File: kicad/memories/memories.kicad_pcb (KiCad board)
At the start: 2 copper layers, 3 parts, among them J1 Conn_01x08, J2 Conn_01x08, U1 NAND512

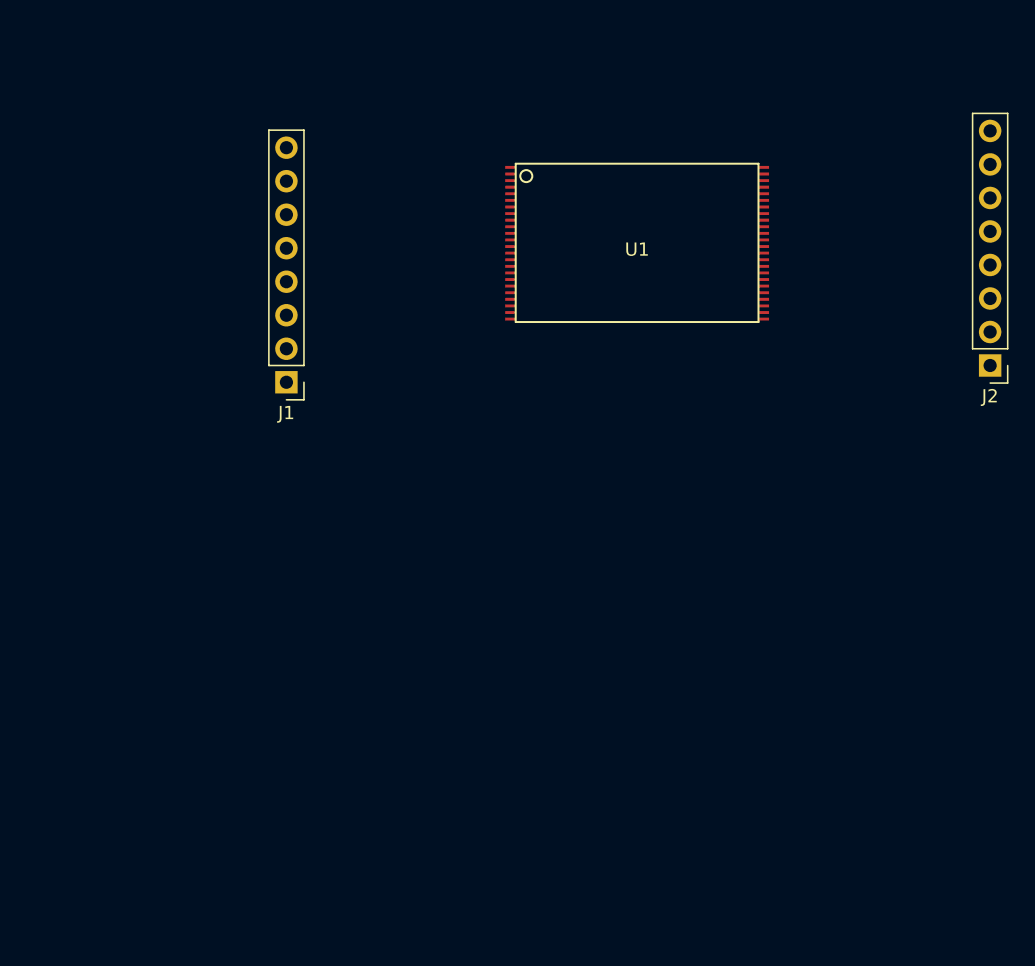
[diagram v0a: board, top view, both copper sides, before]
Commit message: kicad: add mojo shield.
It contains SDRAM, Flash, VGA and PS2.
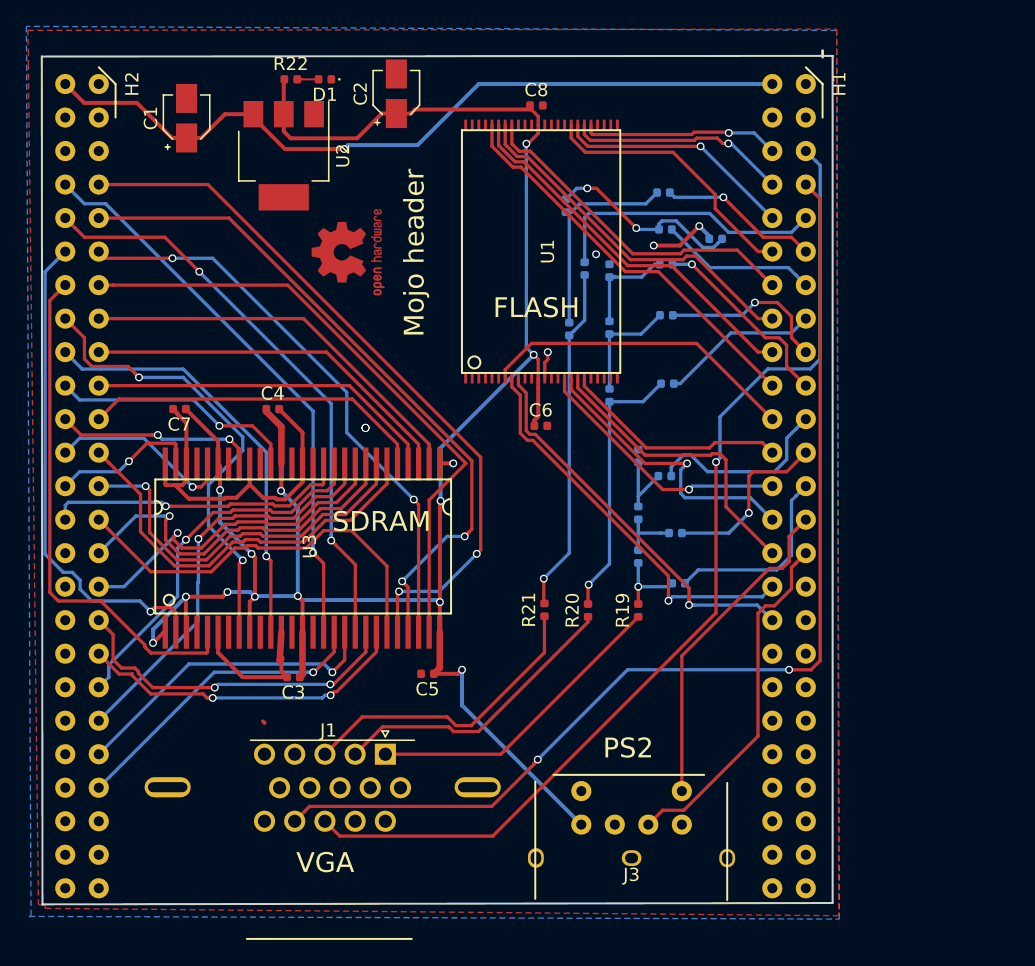
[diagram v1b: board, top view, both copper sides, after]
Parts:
- removed J2: Conn_01x08, Pin_Headers:Pin_Header_Straight_1x08_Pitch2.54mm
- added C1: CP1, Capacitor_SMD:CP_Elec_3x5.3, F.Cu at (114.4, 95.6)
- added C2: CP1, Capacitor_SMD:CP_Elec_3x5.3, F.Cu at (130.3, 93.7)
- added C3: C, Capacitor_SMD:C_0402_1005Metric, F.Cu at (122.5, 137.9)
- added C4: C, Capacitor_SMD:C_0402_1005Metric, F.Cu at (120.9, 117.6)
- added C5: C, Capacitor_SMD:C_0402_1005Metric, F.Cu at (132.6, 137.7)
- added C6: C, Capacitor_SMD:C_0402_1005Metric, F.Cu at (141.2, 118.9)
- added C7: C, Capacitor_SMD:C_0402_1005Metric, F.Cu at (113.8, 117.6)
- added C8: C, Capacitor_SMD:C_0402_1005Metric, F.Cu at (140.9, 94.6)
- added D1: LED, LED_SMD:LED_0402_1005Metric, F.Cu at (124.8, 92.6)
- added H1: Header, memories:mojo_header, F.Cu at (146.1, 100.6)
- added H2: mojo_header_lower, memories:mojo_header, F.Cu at (92.5, 100.6)
- added J3: DIN-6, memories:mini-DIN6, F.Cu at (148.1, 147.8)
- added R1: R, Resistor_SMD:R_0402_1005Metric, B.Cu at (150.6, 122.7)
- added R10: R, Resistor_SMD:R_0402_1005Metric, B.Cu at (151.4, 127.0)
- added R11: R, Resistor_SMD:R_0402_1005Metric, B.Cu at (150.7, 110.5)
- added R12: R, Resistor_SMD:R_0402_1005Metric, B.Cu at (150.5, 101.2)
- added R13: R, Resistor_SMD:R_0402_1005Metric, B.Cu at (148.6, 128.8)
- added R14: R, Resistor_SMD:R_0402_1005Metric, B.Cu at (146.4, 116.6)
- added R15: R, Resistor_SMD:R_0402_1005Metric, B.Cu at (143.4, 111.5)
- added R16: R, Resistor_SMD:R_0402_1005Metric, B.Cu at (151.6, 130.8)
- added R17: R, Resistor_SMD:R_0402_1005Metric, B.Cu at (150.8, 115.7)
- added R18: R, Resistor_SMD:R_0402_1005Metric, B.Cu at (144.5, 107.0)
- added R19: R, Resistor_SMD:R_0402_1005Metric, F.Cu at (148.6, 132.9)
- added R2: R, Resistor_SMD:R_0402_1005Metric, B.Cu at (148.6, 121.2)
- added R20: R, Resistor_SMD:R_0402_1005Metric, F.Cu at (144.8, 132.9)
- added R21: R, Resistor_SMD:R_0402_1005Metric, F.Cu at (141.5, 132.8)
- added R22: R, Resistor_SMD:R_0402_1005Metric, F.Cu at (122.2, 92.6)
- added R3: R, Resistor_SMD:R_0402_1005Metric, B.Cu at (150.7, 106.6)
- added R4: R, Resistor_SMD:R_0402_1005Metric, B.Cu at (146.4, 107.1)
- added R5: R, Resistor_SMD:R_0402_1005Metric, B.Cu at (150.6, 104.0)
- added R6: R, Resistor_SMD:R_0402_1005Metric, B.Cu at (154.5, 104.7)
- added R7: R, Resistor_SMD:R_0402_1005Metric, B.Cu at (148.6, 125.5)
- added R8: R, Resistor_SMD:R_0402_1005Metric, B.Cu at (146.4, 111.4)
- added R9: R, Resistor_SMD:R_0402_1005Metric, B.Cu at (143.1, 102.2)
- added REF**: OSHW-Logo2_7.3x6mm_Copper, Symbol:OSHW-Logo2_7.3x6mm_Copper, F.Cu at (126.6, 105.7)
- added U2: AMS1117-3V3, Package_TO_SOT_SMD:SOT-223, F.Cu at (121.7, 98.4)
- added U3: MT48LC32M8A2, memories:TSOP_54, F.Cu at (123.2, 128.0)
- J1: value Conn_01x08 -> DB15_Female_HighDensity; footprint Pin_Headers:Pin_Header_Straight_1x08_Pitch2.54mm -> memories:DSUB-15-HD_Female
- moved J1 29.2 mm to (129.4, 143.8), turned to 0 degrees
- moved U1 7.31 mm to (141.2, 105.7), turned to 90 degrees
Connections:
- J1 pad 1: Net-(J1-Pad1) -> /VGA/VGA_R_OUT
- J1 pad 2: Net-(J1-Pad2) -> /VGA/VGA_G_OUT
- J1 pad 3: Net-(J1-Pad3) -> /VGA/VGA_B_OUT
- J1 pad 4: Net-(J1-Pad4) -> (no net)
- J1 pad 5: Net-(J1-Pad5) -> GND
- J1 pad 6: Net-(J1-Pad6) -> GND
- J1 pad 7: /GND -> GND
- J1 pad 8: /VCC -> GND
- U1 pad 12: /VCC -> 3V3
- U1 pad 13: /GND -> GND
- U1 pad 16: Net-(J1-Pad2) -> Net-(H1-Pad38)
- U1 pad 17: Net-(J1-Pad3) -> Net-(H1-Pad39)
- U1 pad 18: Net-(J1-Pad4) -> Net-(H1-Pad40)
- U1 pad 19: Net-(J1-Pad1) -> Net-(H1-Pad37)
- U1 pad 36: /GND -> GND
- U1 pad 37: /VCC -> 3V3
- U1 pad 7: (no net) -> Net-(H1-Pad36)
- U1 pad 8: Net-(J1-Pad5) -> Net-(H1-Pad41)
- U1 pad 9: Net-(J1-Pad6) -> Net-(H1-Pad42)
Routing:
- net 3V3: track 0.00 -> 163.4 mm, vias 0 -> 13
- net /VGA/VGA_VSYNC: track 0.00 -> 81.4 mm, vias 0 -> 2
- net /VGA/VGA_HSYNC: track 0.00 -> 77.7 mm, vias 0 -> 1
- net V_EXTERNAL: track 0.00 -> 59.3 mm, vias 0 -> 1
- net Net-(H2-Pad4): track 0.00 -> 55.2 mm, vias 0 -> 2
- net Net-(H2-Pad5): track 0.00 -> 52.0 mm, vias 0 -> 2
- net GND: track 0.00 -> 48.7 mm, vias 0 -> 8
- net Net-(H2-Pad7): track 0.00 -> 47.4 mm
- net Net-(H2-Pad30): track 0.00 -> 44.1 mm, vias 0 -> 2
- net Net-(H2-Pad6): track 0.00 -> 43.7 mm, vias 0 -> 2
- net Net-(H2-Pad29): track 0.00 -> 43.0 mm, vias 0 -> 1
- net /DQ1: track 0.00 -> 39.3 mm
- net /DQ0: track 0.00 -> 37.5 mm, vias 0 -> 1
- net /DQ2: track 0.00 -> 35.2 mm, vias 0 -> 2
- net /DQ3: track 0.00 -> 32.2 mm, vias 0 -> 1
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- added copper zone on B.Cu, net GND
- added copper zone on F.Cu, net GND
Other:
- board outline added: 59.9 x 64.3 mm
- net class Default: clearance 0.2 -> 0.15; trace_width 0.25 -> 0.15
- net class PWR added: clearance 0.15, trace_width 0.3, via_dia 0.6, via_drill 0.4
- rule trace_clearance: 0.2 -> 0.15
- rule trace_min: 0.2 -> 0.15
- board text added: "FLASH"
- board text added: "Mojo header"
- board text added: "PS2"
- board text added: "SDRAM"
- board text added: "VGA"

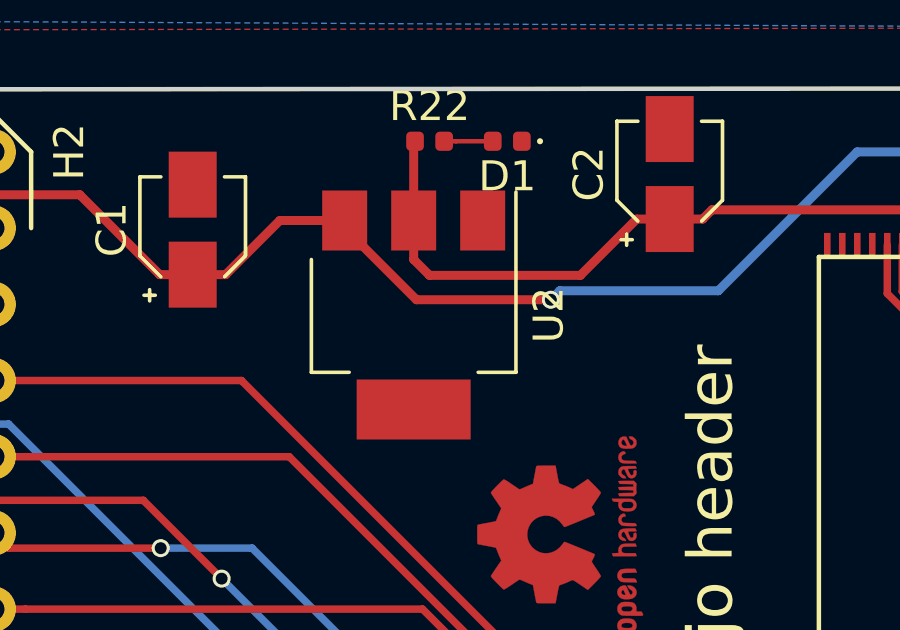
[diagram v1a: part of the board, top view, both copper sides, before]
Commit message: Fix AMS1117 pad net.
In the original datasheet is not indicated that the bigger pad is vout
and not ground how any sensible human could think.
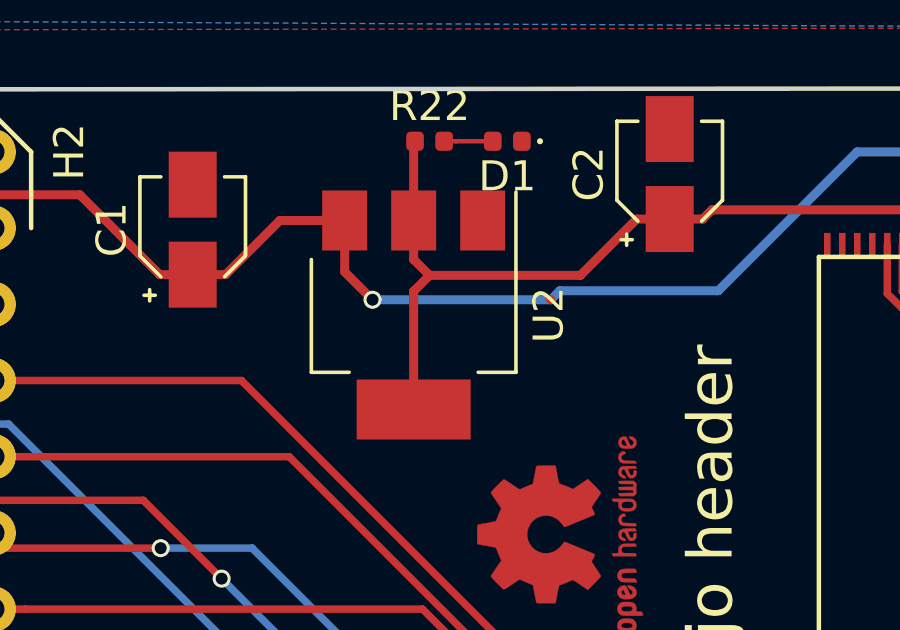
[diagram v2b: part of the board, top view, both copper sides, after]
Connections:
- U2 pad 4: GND -> 3V3
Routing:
- net 3V3: track 163.4 -> 168.1 mm
- net V_EXTERNAL: track 59.3 -> 60.4 mm

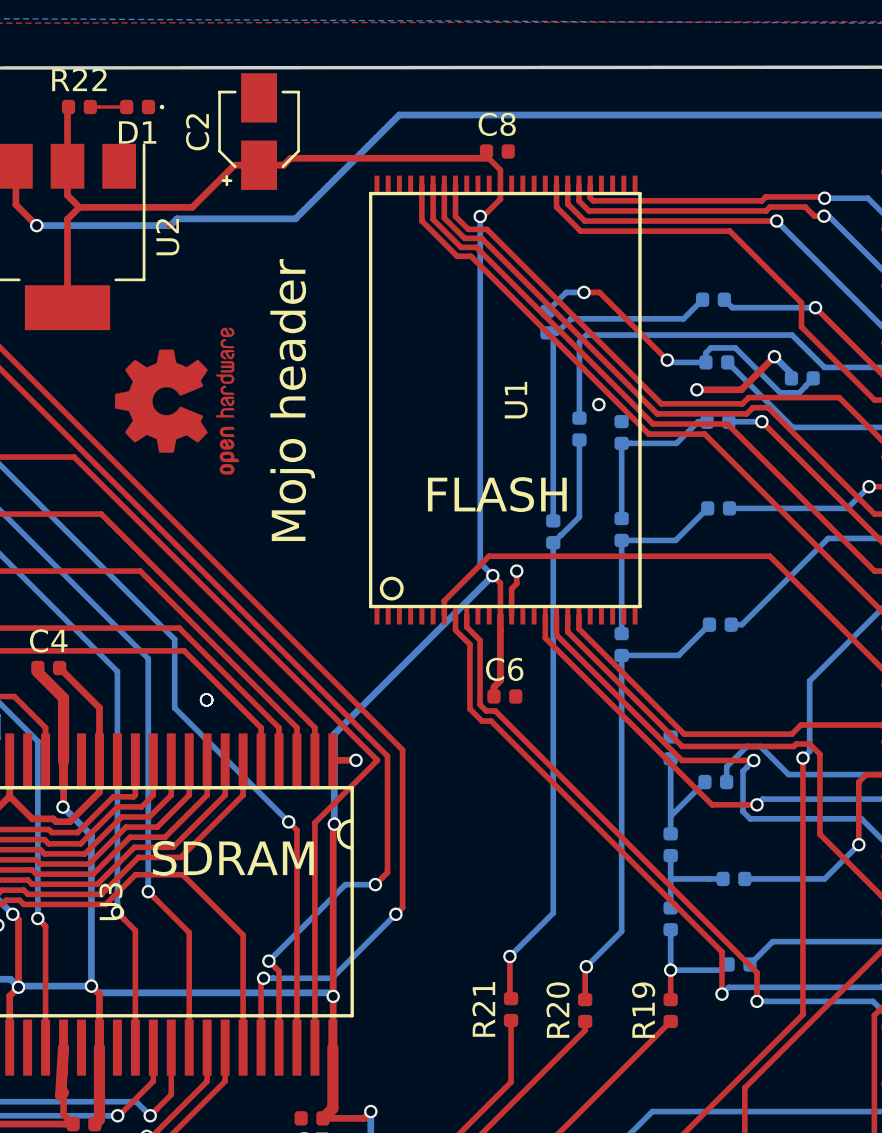
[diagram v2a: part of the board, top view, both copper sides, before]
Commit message: kicad: improve info about memories board.
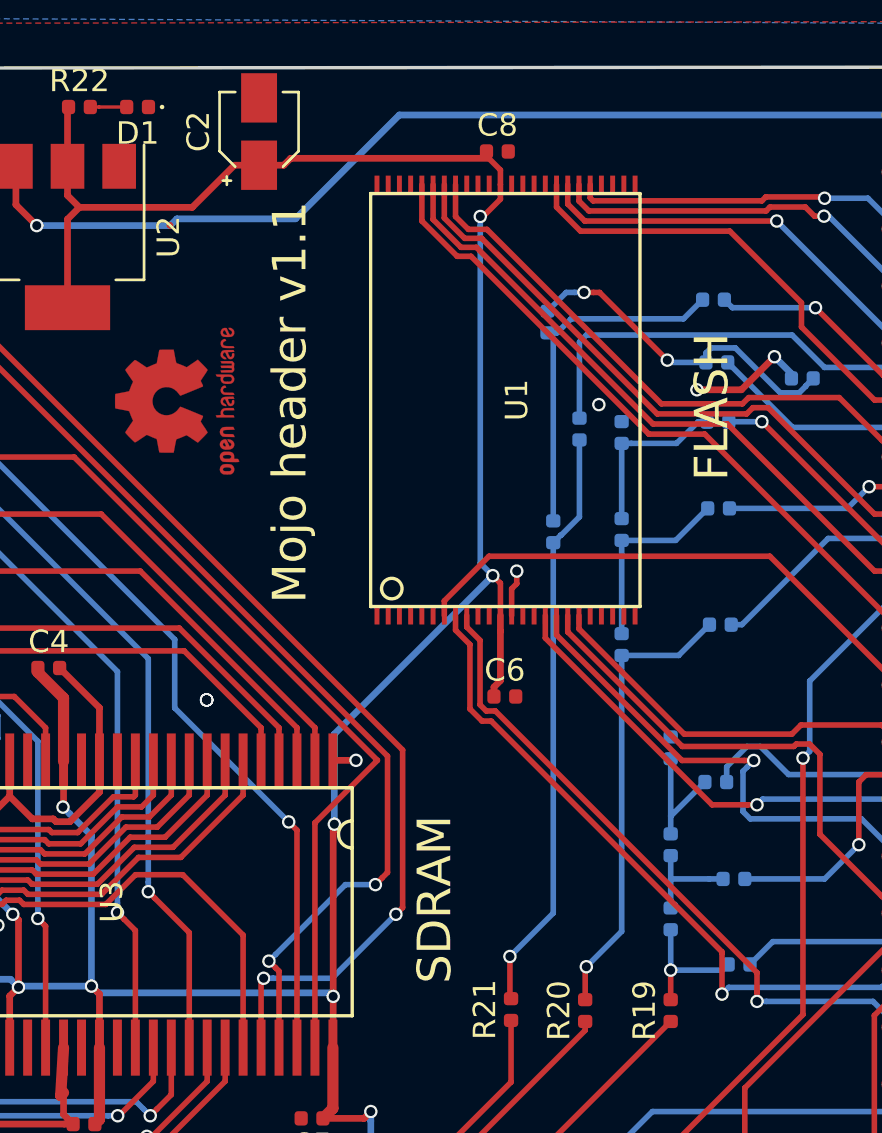
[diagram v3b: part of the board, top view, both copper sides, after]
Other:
- board text added: "Mojo header v1.1"
- board text removed: "Mojo header"
